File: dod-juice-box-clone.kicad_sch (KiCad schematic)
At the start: 0 parts

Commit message: Progress
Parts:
- added C1: 100nF, Capacitor_THT:CP_Radial_D6.3mm_P2.50mm, symbol Device:C_Small
- added C10: 47nF, Capacitor_THT:C_Rect_L7.2mm_W2.5mm_P5.00mm_FKS2_FKP2_MKS2_MKP2, symbol Device:C_Small
- added C11, C12, C15, C2, C5, C6: 10nF, Capacitor_THT:C_Rect_L7.2mm_W2.5mm_P5.00mm_FKS2_FKP2_MKS2_MKP2, symbol Device:C_Small
- added C13: 2.2nF, Capacitor_THT:C_Rect_L7.2mm_W2.5mm_P5.00mm_FKS2_FKP2_MKS2_MKP2, symbol Device:C_Small
- added C14: 1uF, symbol Device:C_Polarized_Small_US
- added C3: 50pF, Capacitor_THT:C_Disc_D3.8mm_W2.6mm_P2.50mm, symbol Device:C_Small
- added C4: 150nF, Capacitor_THT:C_Rect_L7.2mm_W2.5mm_P5.00mm_FKS2_FKP2_MKS2_MKP2, symbol Device:C_Small
- added C7: 220nF, Capacitor_THT:CP_Radial_D6.3mm_P2.50mm, symbol Device:C_Small
- added C8, C9: 10uF, symbol Device:C_Polarized_Small_US
- added D3, D5: 1N4148, Diode_THT:D_DO-35_SOD27_P7.62mm_Horizontal, symbol Diode:1N4148
- added D4: 1N4001, Diode_THT:D_DO-41_SOD81_P10.16mm_Horizontal, symbol Diode:1N4001
- added H1: PWR_IN, MountingHole:MountingHole_2.2mm_M2_DIN965_Pad_TopBottom, symbol Mechanical:MountingHole_Pad
- added H10: SW_OUT, MountingHole:MountingHole_2.2mm_M2_DIN965_Pad_TopBottom, symbol Mechanical:MountingHole_Pad
- added H11: SW_GND, MountingHole:MountingHole_2.2mm_M2_DIN965_Pad_TopBottom, symbol Mechanical:MountingHole_Pad
- added H12: SW_LED, MountingHole:MountingHole_2.2mm_M2_DIN965_Pad_TopBottom, symbol Mechanical:MountingHole_Pad
- added H2: PWR_GND, MountingHole:MountingHole_2.2mm_M2_DIN965_Pad_TopBottom, symbol Mechanical:MountingHole_Pad
- added H3: INPUT_IN, MountingHole:MountingHole_2.2mm_M2_DIN965_Pad_TopBottom, symbol Mechanical:MountingHole_Pad
- added H4: INPUT_GND, MountingHole:MountingHole_2.2mm_M2_DIN965_Pad_TopBottom, symbol Mechanical:MountingHole_Pad
- added H5: SW_IN, MountingHole:MountingHole_2.2mm_M2_DIN965_Pad_TopBottom, symbol Mechanical:MountingHole_Pad
- added H6: SW_SEND, MountingHole:MountingHole_2.2mm_M2_DIN965_Pad_TopBottom, symbol Mechanical:MountingHole_Pad
- added H7: SW_RTN, MountingHole:MountingHole_2.2mm_M2_DIN965_Pad_TopBottom, symbol Mechanical:MountingHole_Pad
- added H8: OUTPUT_OUT, MountingHole:MountingHole_2.2mm_M2_DIN965_Pad_TopBottom, symbol Mechanical:MountingHole_Pad
- added H9: OUTPUT_GND, MountingHole:MountingHole_2.2mm_M2_DIN965_Pad_TopBottom, symbol Mechanical:MountingHole_Pad
- added Q1: J201, symbol Device:Q_NJFET_DSG
- added Q2, Q3: 2N5088, Package_TO_SOT_THT:TO-92_Inline, symbol Transistor_BJT:2N3904
- added R1: 1MΩ, Resistor_THT:R_Axial_DIN0207_L6.3mm_D2.5mm_P7.62mm_Horizontal, symbol Device:R_Small_US
- added R10, R14, R17, R19, R2, R20, R7: 10kΩ, Resistor_THT:R_Axial_DIN0207_L6.3mm_D2.5mm_P7.62mm_Horizontal, symbol Device:R_Small_US
- added R11, R13: 220kΩ, Resistor_THT:R_Axial_DIN0207_L6.3mm_D2.5mm_P7.62mm_Horizontal, symbol Device:R_Small_US
- added R12: 6.8kΩ, Resistor_THT:R_Axial_DIN0207_L6.3mm_D2.5mm_P7.62mm_Horizontal, symbol Device:R_Small_US
- added R15: 47kΩ, Resistor_THT:R_Axial_DIN0207_L6.3mm_D2.5mm_P7.62mm_Horizontal, symbol Device:R_Small_US
- added R16: 100kΩ, Resistor_THT:R_Axial_DIN0207_L6.3mm_D2.5mm_P7.62mm_Horizontal, symbol Device:R_Small_US
- added R18: 15kΩ, Resistor_THT:R_Axial_DIN0207_L6.3mm_D2.5mm_P7.62mm_Horizontal, symbol Device:R_Small_US
- added R3: 470kΩ, Resistor_THT:R_Axial_DIN0207_L6.3mm_D2.5mm_P7.62mm_Horizontal, symbol Device:R_Small_US
- added R4: 150kΩ, Resistor_THT:R_Axial_DIN0207_L6.3mm_D2.5mm_P7.62mm_Horizontal, symbol Device:R_Small_US
- added R5: 2kΩ, Resistor_THT:R_Axial_DIN0207_L6.3mm_D2.5mm_P7.62mm_Horizontal, symbol Device:R_Small_US
- added R6: 22kΩ, Resistor_THT:R_Axial_DIN0207_L6.3mm_D2.5mm_P7.62mm_Horizontal, symbol Device:R_Small_US
- added R8, R9: 4.7kΩ, Resistor_THT:R_Axial_DIN0207_L6.3mm_D2.5mm_P7.62mm_Horizontal, symbol Device:R_Small_US
- added RV1, RV2, RV3, RV4: W100K, Potentiometer_THT:Potentiometer_Omeg_PC16BU_Vertical, symbol Device:R_Potentiometer_Small
- added U1: RC4558, symbol Amplifier_Operational:RC4558
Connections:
- new net: R6.2, RV2.1, U1.5 (+)
- new net: C4.2, RV2.2
- new net: C11.1, C12.2, R15.1, RV2.3, U1.6 (-)
- new net: R19.2, R20.1, RV3.1
- new net: C15.2, RV3.2
- new net: C13.1, Q3.2 (B), R16.2
- new net: C11.2, C14.1, R15.2, U1.7
- new net: Q2.1 (E), R12.1, R14.2
- new net: C4.1, C6.2, R12.2
- new net: C2.2, R2.1, R3.1
- new net: C3.2, C5.1, D3.1 (K), D5.2 (A), R4.2, U1.1
- new net: R2.2, U1.2 (-)
- new net: C3.1, D3.2 (A), D5.1 (K), R4.1, RV1.3, U1.3 (+)
- new net: C14.2, R19.1
- new net: H10.1, H8.1
- new net: C10.1, R10.2
- new net: C10.2, Q1.3 (G), R1.1
- new net: C7.2, R5.1
- new net: R5.2, RV1.1, RV1.2
- new net: C5.2, R11.2, R6.1
- new net: Q3.1 (E), R17.2, R18.1
- new net: C12.1, C13.2, R18.2
- new net: C2.1, Q1.2 (S), R7.1
- new net: C6.1, Q2.2 (B), R13.2
- new net: R20.2, RV4.3
- new net: H3.1, H5.1
- new net +4.5V: C1.1, C15.1, C8.1, R1.2, R11.1, R13.1, R16.1, R3.2, R8.2, R9.2, RV3.3, RV4.1, U1.8 (V+)
- new net +9V: C9.1, D4.1 (K), H1.1, H12.1, Q1.1 (D), Q2.3 (C), Q3.3 (C), R8.1
- new net GND: C1.2, C7.1, C8.2, C9.2, D4.2 (A), H11.1, H2.1, H4.1, H9.1, R14.1, R17.1, R7.2, R9.1, U1.4 (V-)
- new net INPUT: H6.1, R10.1
- new net OUTPUT: H7.1
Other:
- note added: "TODO: add clean blend"
- note added: "TODO: figure out how much of circuit is switching"

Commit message: Finished schematic?
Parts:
- added C16, C17: 1uF, symbol Device:C_Polarized_Small_US
- added Q4: 2N5088, Package_TO_SOT_THT:TO-92_Inline, symbol Transistor_BJT:2N3904
- added R21: 7.5kΩ, Resistor_THT:R_Axial_DIN0207_L6.3mm_D2.5mm_P7.62mm_Horizontal, symbol Device:R_Small_US
- added R22: 4.7kΩ, Resistor_THT:R_Axial_DIN0207_L6.3mm_D2.5mm_P7.62mm_Horizontal, symbol Device:R_Small_US
- added R23: 10kΩ, Resistor_THT:R_Axial_DIN0207_L6.3mm_D2.5mm_P7.62mm_Horizontal, symbol Device:R_Small_US
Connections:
- net +9V: now also Q4.3 (C)
- net GND: now also R22.1
- net OUTPUT: now also C16.2
- net at C2.1, Q1.2 (S), R7.1: now also Q4.2 (B)
- net at RV4.2: now also C16.1
- net at R20.2, RV4.3: now also R23.2
- new net: Q4.1 (E), R21.2
- new net: C17.1, R21.1, R22.2
- new net: C17.2, R23.1
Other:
- note removed: "TODO: add clean blend"
- note removed: "TODO: figure out how much of circuit is switching"
- moved on the sheet: C1, C10, C11, C12, C13, C14, C15, C2, C3, C4, C5, C6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

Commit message: Add footprints
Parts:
- C1, C7: footprint Capacitor_THT:CP_Radial_D6.3mm_P2.50mm -> Capacitor_THT:C_Rect_L7.2mm_W2.5mm_P5.00mm_FKS2_FKP2_MKS2_MKP2
- C14, C16, C17, C8, C9: footprint (none) -> Capacitor_THT:CP_Radial_D6.3mm_P2.50mm
- Q1: footprint (none) -> Package_TO_SOT_THT:TO-92_Inline
- U1: footprint (none) -> Package_DIP:DIP-8_W7.62mm
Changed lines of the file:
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@@
 			)
 		)
-		(property "Footprint" ""
+		(property "Footprint" "Capacitor_THT:CP_Radial_D6.3mm_P2.50mm"
 			(at 247.65 33.02 0)
 			(effects
@@
 			)
 		)
-		(property "Footprint" ""
+		(property "Footprint" "Package_DIP:DIP-8_W7.62mm"
 			(at 245.11 63.5 0)
 			(effects
@@
 			)
 		)
-		(property "Footprint" ""
+		(property "Footprint" "Package_DIP:DIP-8_W7.62mm"
 			(at 140.97 60.96 0)
 			(effects
@@
 			)
 		)
-		(property "Footprint" ""
+		(property "Footprint" "Package_DIP:DIP-8_W7.62mm"
 			(at 266.7 30.48 0)
 			(effects
@@
 			)
 		)
-		(property "Footprint" ""
+		(property "Footprint" "Capacitor_THT:CP_Radial_D6.3mm_P2.50mm"
 			(at 261.62 63.5 0)
 			(effects
@@
 			)
 		)
-		(property "Footprint" ""
+		(property "Footprint" "Capacitor_THT:CP_Radial_D6.3mm_P2.50mm"
 			(at 306.07 100.33 0)
 			(effects
@@
 			)
 		)
-		(property "Footprint" ""
+		(property "Footprint" "Capacitor_THT:CP_Radial_D6.3mm_P2.50mm"
 			(at 118.11 125.73 0)
 			(effects
@@
 			)
 		)
-		(property "Footprint" ""
+		(property "Footprint" "Package_TO_SOT_THT:TO-92_Inline"
 			(at 64.77 55.88 0)
 			(effects
@@
 			)
 		)
-		(property "Footprint" ""
+		(property "Footprint" "Capacitor_THT:CP_Radial_D6.3mm_P2.50mm"
 			(at 214.63 33.02 0)
 			(effects
@@
 			)
 		)
-		(property "Footprint" "Capacitor_THT:CP_Radial_D6.3mm_P2.50mm"
+		(property "Footprint" "Capacitor_THT:C_Rect_L7.2mm_W2.5mm_P5.00mm_FKS2_FKP2_MKS2_MKP2"
 			(at 90.17 41.91 0)
 			(effects
@@
 			)
 		)
-		(property "Footprint" "Capacitor_THT:CP_Radial_D6.3mm_P2.50mm"
+		(property "Footprint" "Capacitor_THT:C_Rect_L7.2mm_W2.5mm_P5.00mm_FKS2_FKP2_MKS2_MKP2"
 			(at 275.59 30.48 0)
 			(effects

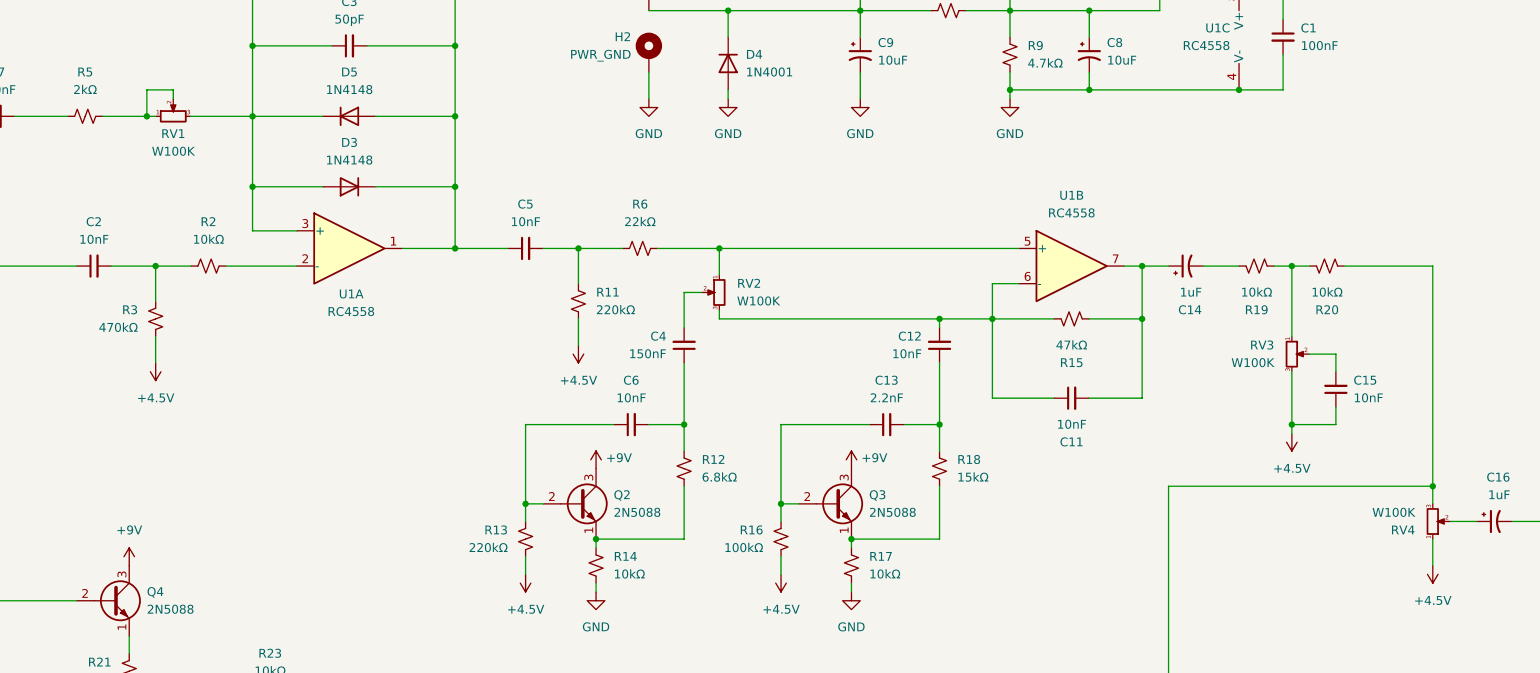
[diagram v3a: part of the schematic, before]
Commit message: Add correct pot component to schematic
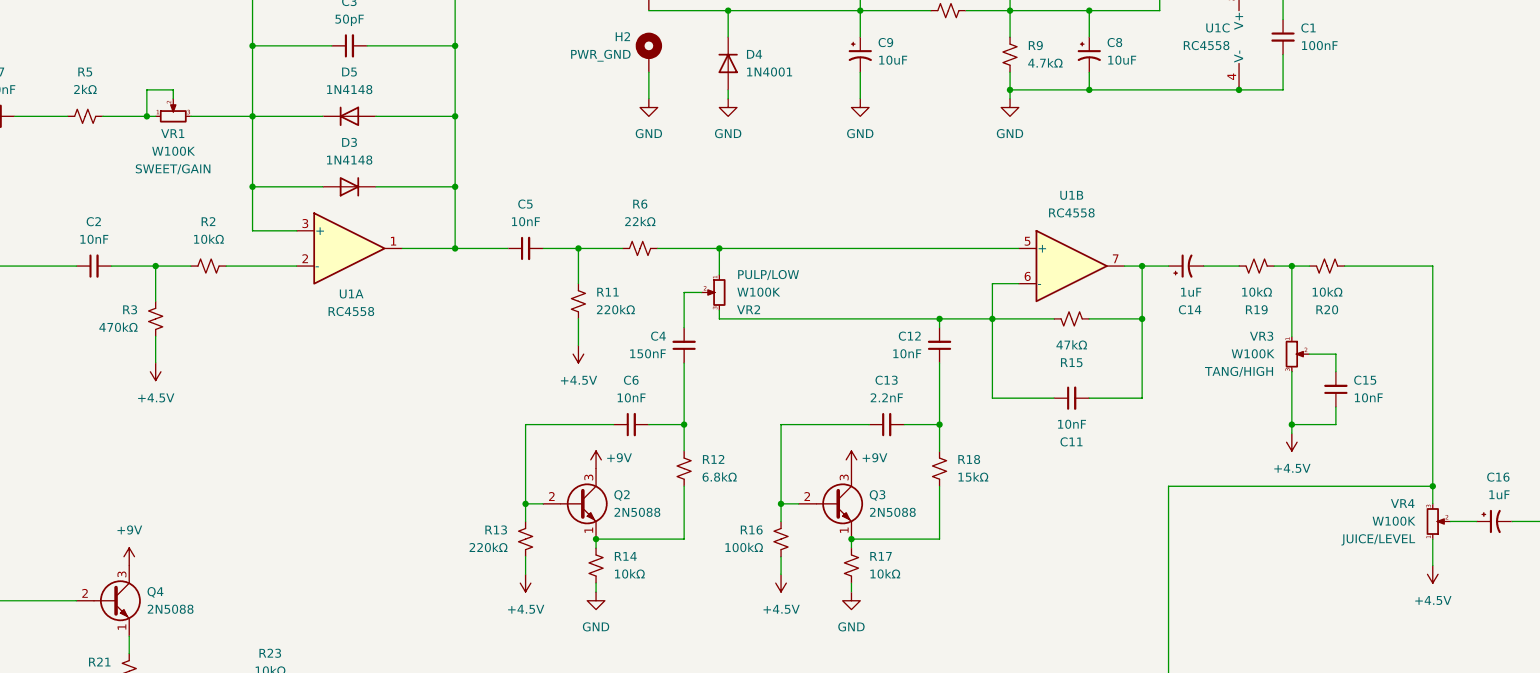
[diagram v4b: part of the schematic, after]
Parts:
- removed RV1, RV2, RV3, RV4: W100K, Potentiometer_THT:Potentiometer_Omeg_PC16BU_Vertical, symbol Device:R_Potentiometer_Small
- added VR1, VR2, VR3, VR4: W100K, Floodlight_Custom_Footprints:Alpha_RV16AF-41, symbol Floodlight_Custom_Symbols:Alpha_RV16AF-41
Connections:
- net +4.5V: now also VR3.3, VR4.1
- net at R6.2, U1.5 (+): now also VR2.1
- net at C4.2: now also VR2.2
- net at C11.1, C12.2, R15.1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: now also VR2.3
- net at R19.2, R20.1: now also VR3.1
- net at C15.2: now also VR3.2
- net at C3.1, D3.2 (A), D5.1 (K)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: now also VR1.3
- net at R5.2: now also VR1.1, VR1.2
- net at C16.1: now also VR4.2
- net at R20.2, R23.2: now also VR4.3
